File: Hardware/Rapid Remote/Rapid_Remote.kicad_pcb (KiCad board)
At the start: 2 copper layers, 34.2 x 61.6 mm, 44 parts, among them J1 Conn_01x02_Socket, U1 MIC5504-3.3YM5, U3 WS4518D, U4 XB6096I2SV, U5 ESP32-C3-MINI-1

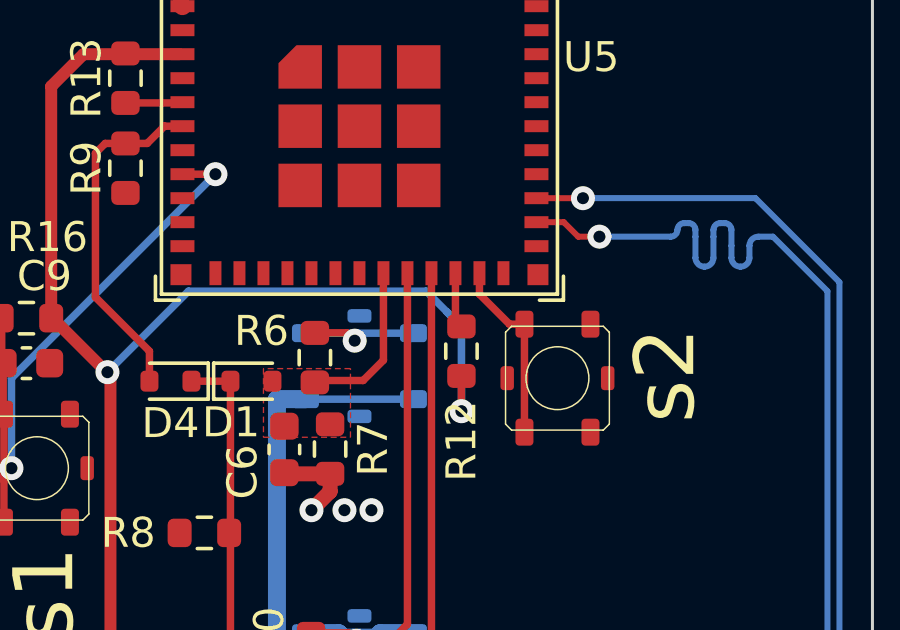
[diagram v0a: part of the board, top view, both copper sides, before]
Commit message: updated to use mounting holes as jig for stencil
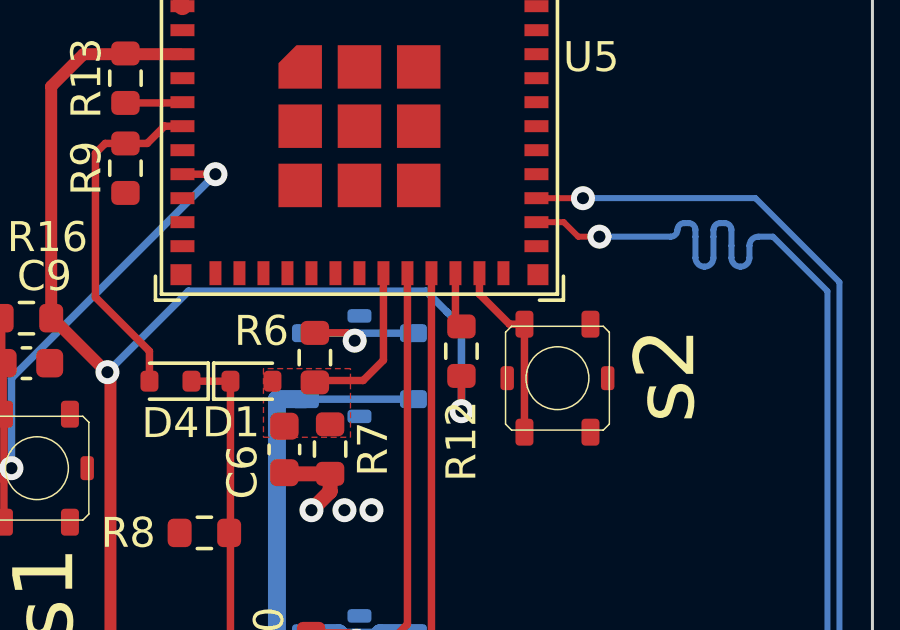
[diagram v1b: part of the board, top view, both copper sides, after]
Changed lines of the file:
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@@
         (effects (font (size 1.27 1.27) (thickness 0.254)))
     )
-    (fp_text user "VBUS" (at -0.75 -2.5 90) (layer "F.SilkS")
+    (fp_text user "DN2" (at 0.75 0.75 90) (layer "F.SilkS")
         (effects (font (size 0.508 0.508) (thickness 0.127)))
     )
-    (fp_text user "GND" (at -1 -3.3655 90) (layer "F.SilkS")
+    (fp_text user "A40-00119-A52-12" (at 2.667 0) (layer "F.SilkS")
         (effects (font (size 0.508 0.508) (thickness 0.127)))
     )
-    (fp_text user "SBU2" (at 1 1.75 90) (layer "F.SilkS")
+    (fp_text user "SBU1" (at 1 -1.25 90) (layer "F.SilkS")
         (effects (font (size 0.508 0.508) (thickness 0.127)))
     )
-    (fp_text user "CC2" (at -1 -1.75 90) (layer "F.SilkS")
+    (fp_text user "DP1" (at -1 0.25 90) (layer "F.SilkS")
         (effects (font (size 0.508 0.508) (thickness 0.127)))
     )
@@
         (effects (font (size 0.508 0.508) (thickness 0.127)))
     )
-    (fp_text user "GND" (at -1 3.3655 90) (layer "F.SilkS")
+    (fp_text user "DN1" (at 0.75 -0.25 90) (layer "F.SilkS")
         (effects (font (size 0.508 0.508) (thickness 0.127)))
     )
-    (fp_text user "DN2" (at 0.75 0.75 90) (layer "F.SilkS")
+    (fp_text user "GND" (at -1 -3.3655 90) (layer "F.SilkS")
         (effects (font (size 0.508 0.508) (thickness 0.127)))
     )
-    (fp_text user "DN1" (at 0.75 -0.25 90) (layer "F.SilkS")
+    (fp_text user "SBU2" (at 1 1.75 90) (layer "F.SilkS")
         (effects (font (size 0.508 0.508) (thickness 0.127)))
     )
-    (fp_text user "SBU1" (at 1 -1.25 90) (layer "F.SilkS")
+    (fp_text user "VBUS" (at -0.75 2.5 90) (layer "F.SilkS")
         (effects (font (size 0.508 0.508) (thickness 0.127)))
     )
-    (fp_text user "DP1" (at -1 0.25 90) (layer "F.SilkS")
+    (fp_text user "GND" (at -1 3.3655 90) (layer "F.SilkS")
         (effects (font (size 0.508 0.508) (thickness 0.127)))
     )
-    (fp_text user "VBUS" (at -0.75 2.5 90) (layer "F.SilkS")
+    (fp_text user "CC2" (at -1 -1.75 90) (layer "F.SilkS")
         (effects (font (size 0.508 0.508) (thickness 0.127)))
     )
-    (fp_text user "A40-00119-A52-12" (at 2.667 0) (layer "F.SilkS")
+    (fp_text user "VBUS" (at -0.75 -2.5 90) (layer "F.SilkS")
         (effects (font (size 0.508 0.508) (thickness 0.127)))
     )
@@
     (pad "B12" smd rect (at -3.932 3.075) (size 0.3 1.15) (layers "F.Cu" "F.Paste" "F.Mask")
       (net 2 "GND") (pinfunction "GND") (pintype "power_in") (solder_paste_margin -0.01))
-    (model "D:/Users/Thomas/Documents/GitHub/ESP32-C3-DevKit-Lipo/HARDWARE/ESP32-C3-DevKit-Lipo_Rev_B/3d/USB4105-GF-A.stp"
-      (offset (xyz 3.75 -16.04 0))
+    (model ":KICAD7_3DMODEL_DIR:Connector_USB.3dshapes/USB_C_Receptacle_GCT_USB4105-xx-A_16P_TopMnt_Horizontal.step"
+      (offset (xyz 0 0 0))
       (scale (xyz 1 1 1))
-      (rotate (xyz -90 0 -90))
+      (rotate (xyz 0 0 -90))
     )
   )
@@
     (pad "P4" smd roundrect (at 1.8 1.1 90) (size 0.9 0.6) (layers "F.Cu" "F.Paste" "F.Mask") (roundrect_rratio 0.2116666667)
       (net 2 "GND") (pinfunction "4") (pintype "bidirectional") (thermal_bridge_angle 45))
-    (model "C:/Users/TomWhyte-Venables/Documents/GitHub/Rapid-Training-Target/Hardware/CAD/ts-1177-c-b-b.stp"
+    (model "D:/Users/Thomas/Documents/GitHub/Rapid-Training-Target/Hardware/CAD/ts-1177-c-b-b.stp"
       (offset (xyz 0 0 0))
       (scale (xyz 1 1 1))
@@
     (pad "P4" smd roundrect (at 1.8 1.1 90) (size 0.9 0.6) (layers "F.Cu" "F.Paste" "F.Mask") (roundrect_rratio 0.2116666667)
       (net 2 "GND") (pinfunction "4") (pintype "bidirectional") (thermal_bridge_angle 45))
-    (model "C:/Users/TomWhyte-Venables/Documents/GitHub/Rapid-Training-Target/Hardware/CAD/ts-1177-c-b-b.stp"
+    (model "D:/Users/Thomas/Documents/GitHub/Rapid-Training-Target/Hardware/CAD/ts-1177-c-b-b.stp"
       (offset (xyz 0 0 0))
       (scale (xyz 1 1 1))
@@
     (pad "P4" smd roundrect (at 1.8 -1.1 180) (size 0.9 0.6) (layers "B.Cu" "B.Paste" "B.Mask") (roundrect_rratio 0.2116666667)
       (net 36 "+3V8") (pinfunction "4") (pintype "bidirectional") (thermal_bridge_angle 45))
-    (model "C:/Users/TomWhyte-Venables/Documents/GitHub/Rapid-Training-Target/Hardware/CAD/ts-1177-c-b-b.stp"
+    (model "D:/Users/Thomas/Documents/GitHub/Rapid-Training-Target/Hardware/CAD/ts-1177-c-b-b.stp"
       (offset (xyz 0 0 0))
       (scale (xyz 1 1 1))
@@
     (pad "P4" smd roundrect (at 1.8 -1.1 180) (size 0.9 0.6) (layers "B.Cu" "B.Paste" "B.Mask") (roundrect_rratio 0.2116666667)
       (net 36 "+3V8") (pinfunction "4") (pintype "bidirectional") (thermal_bridge_angle 45))
-    (model "C:/Users/TomWhyte-Venables/Documents/GitHub/Rapid-Training-Target/Hardware/CAD/ts-1177-c-b-b.stp"
+    (model "D:/Users/Thomas/Documents/GitHub/Rapid-Training-Target/Hardware/CAD/ts-1177-c-b-b.stp"
       (offset (xyz 0 0 0))
       (scale (xyz 1 1 1))
@@
     (pad "P4" smd roundrect (at 1.8 -1.1 180) (size 0.9 0.6) (layers "B.Cu" "B.Paste" "B.Mask") (roundrect_rratio 0.2116666667)
       (net 36 "+3V8") (pinfunction "4") (pintype "bidirectional") (thermal_bridge_angle 45))
-    (model "C:/Users/TomWhyte-Venables/Documents/GitHub/Rapid-Training-Target/Hardware/CAD/ts-1177-c-b-b.stp"
+    (model "D:/Users/Thomas/Documents/GitHub/Rapid-Training-Target/Hardware/CAD/ts-1177-c-b-b.stp"
       (offset (xyz 0 0 0))
       (scale (xyz 1 1 1))
@@
     )
   )
+  (gr_circle (center 138 93.9) (end 139.5 93.9)
+    (stroke (width 0.2) (type solid)) (fill solid) (layer "B.Paste"))
+  (gr_circle (center 165.2 121.2) (end 166.7 121.2)
+    (stroke (width 0.2) (type solid)) (fill solid) (layer "B.Paste"))
+  (gr_circle (center 165.2 66.6) (end 166.7 66.6)
+    (stroke (width 0.2) (type solid)) (fill solid) (layer "B.Paste"))
+  (gr_circle (center 138 93.9) (end 139.5 93.9)
+    (stroke (width 0.2) (type solid)) (fill solid) (layer "F.Paste"))
+  (gr_circle (center 165.2 121.2) (end 166.7 121.2)
+    (stroke (width 0.2) (type solid)) (fill solid) (layer "F.Paste"))
+  (gr_circle (center 165.2 66.6) (end 166.7 66.6)
+    (stroke (width 0.2) (type solid)) (fill solid) (layer "F.Paste"))
   (gr_poly locked
     (pts
@@
   (via (at 143.2 82.4) (size 0.8) (drill 0.4) (layers "F.Cu" "B.Cu") (net 10))
   (segment (start 145.9 79.7) (end 143.2 82.4) (width 0.25) (layer "B.Cu") (net 10))
-  (segment (start 154.7245 80.6) (end 154.51225 80.38775) (width 0.25) (layer "B.Cu") (net 10))
   (segment (start 154.51225 80.38775) (end 153.8245 79.7) (width 0.25) (layer "B.Cu") (net 10))
   (segment (start 154.51225 80.38775) (end 155 80.8755) (width 0.25) (layer "B.Cu") (net 10))

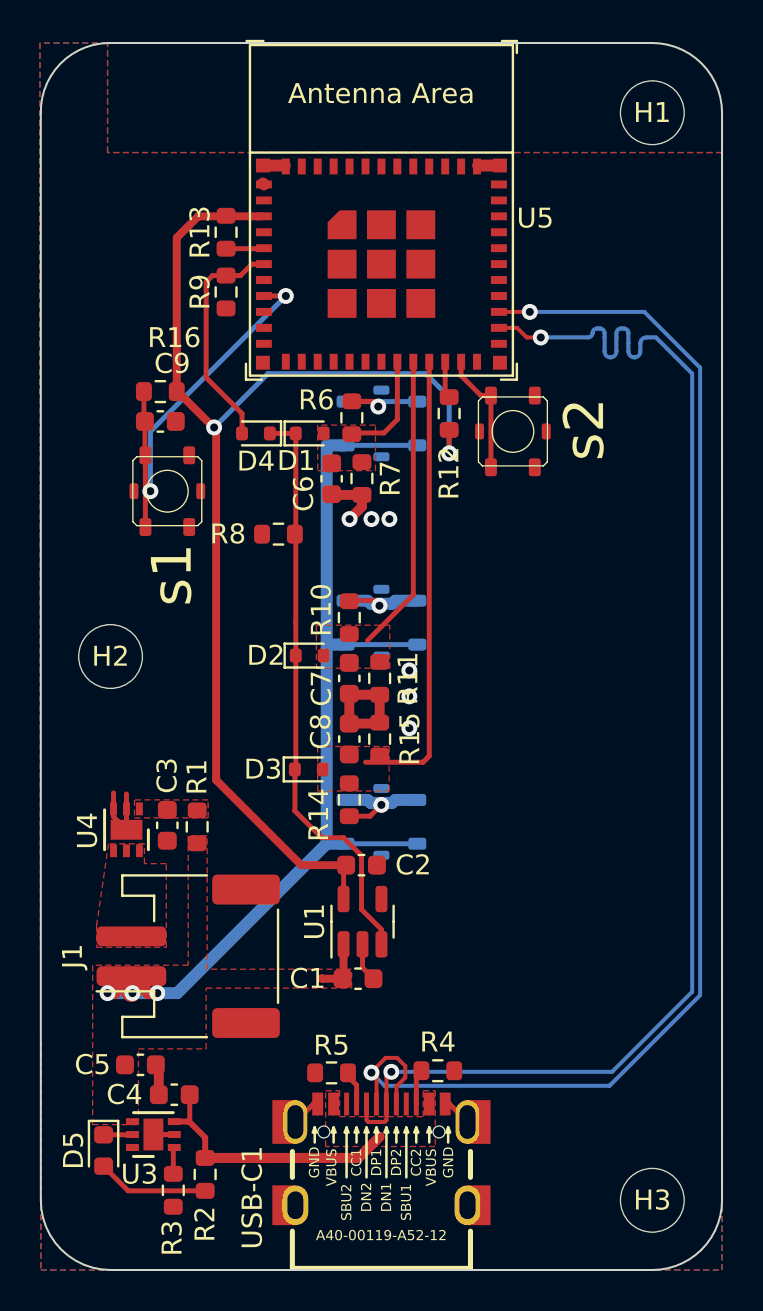
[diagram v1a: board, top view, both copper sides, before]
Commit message: Updated Footprints for LED
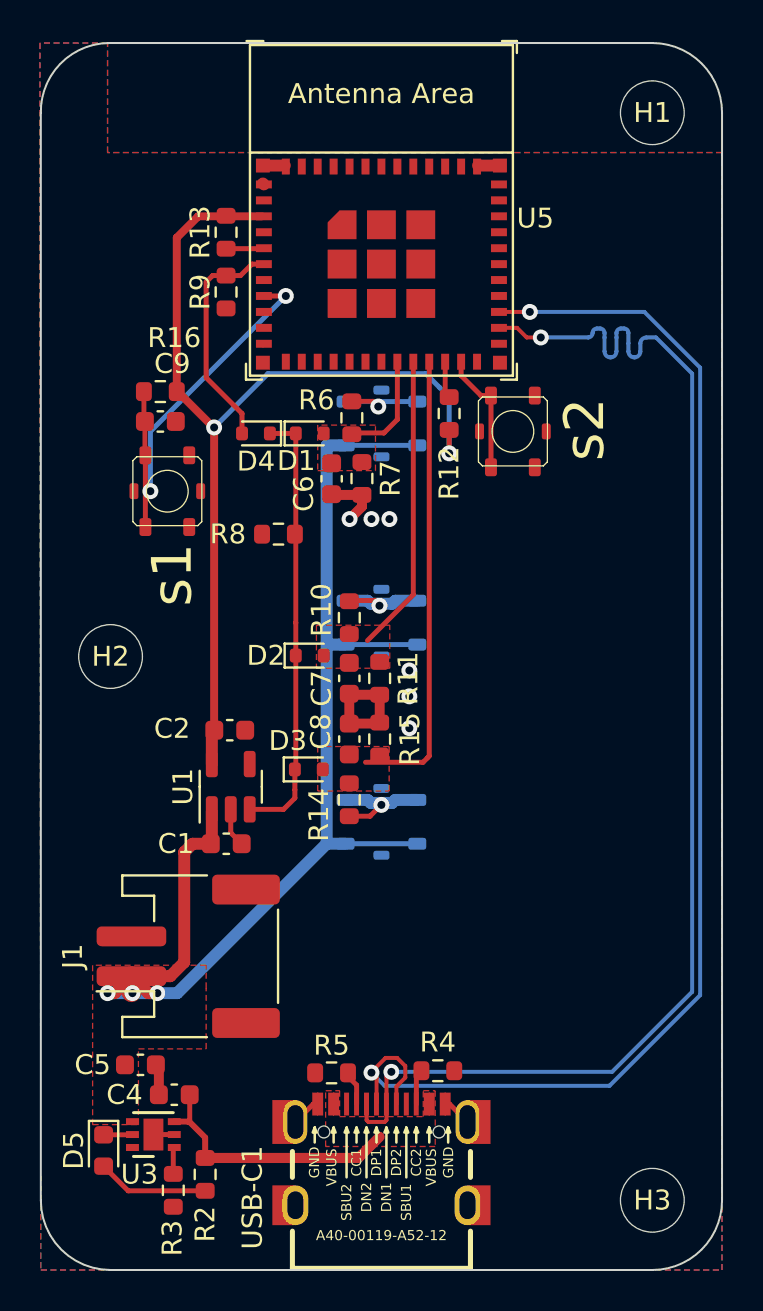
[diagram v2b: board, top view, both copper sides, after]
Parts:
- removed C3: 100n, Capacitor_SMD:C_0603_1608Metric
- removed R1: 1k, Resistor_SMD:R_0603_1608Metric
- removed U4: XB6096I2SV, Package_DFN_QFN:DFN-6-1EP_2x2mm_P0.65mm_EP1x1.6mm
- R3: value 47.5k -> 5k
- moved C1 9.47 mm to (143.8, 103.3)
- moved U1 9.47 mm to (144.0, 100.4)
- moved C2 9.47 mm to (144.0, 97.6)
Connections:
- J1 pad 2: Net-(J1-Pin_2) -> GND
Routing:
- net +3V3: track 60.2 -> 49.7 mm
- net +3V8: track 55.0 -> 63.9 mm
- net EN_LDO: track 29.0 -> 21.7 mm
- net GND: track 23.2 -> 19.3 mm
- removed copper zone on F.Cu, net Net-(J1-Pin_2)
- removed copper zone on F.Cu, net Net-(U4-VDD)
